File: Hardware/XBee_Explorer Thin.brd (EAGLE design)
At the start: 45.7 x 54.6 mm, 129 parts, among them J4 QWIIC_RIGHT_ANGLE, Q2 3.1A/30V/105mΩ, U1 FSUSB30MUX_MSOP10, U2 AP63203, U3 ESD Diode, U5 ESD Diode, U6 CP210X

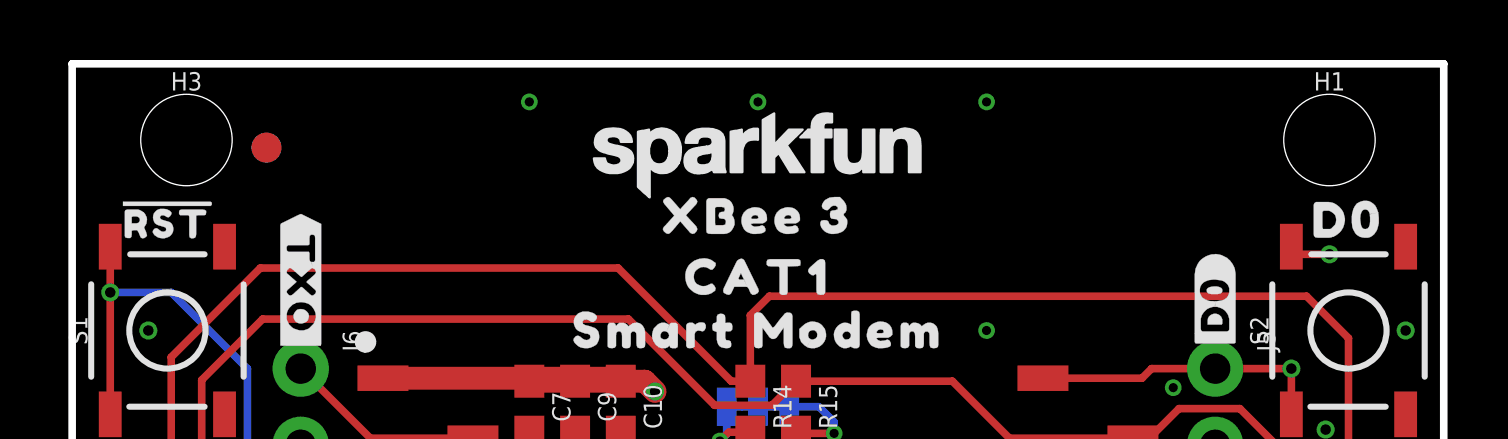
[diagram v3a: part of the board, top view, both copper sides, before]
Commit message: Fixes mounting holes being off grid
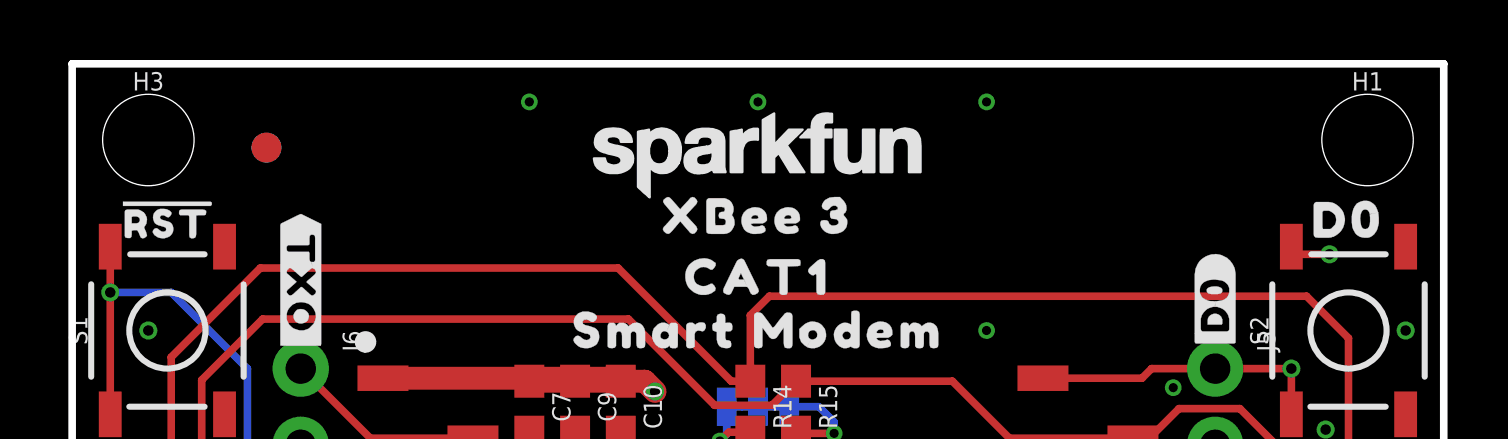
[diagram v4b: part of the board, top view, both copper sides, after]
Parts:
- moved H3 1.27 mm to (1.27, 52.1)
- moved H1 1.27 mm to (41.9, 52.1)
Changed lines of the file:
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@@
 <layer number="37" name="tTest" color="7" fill="1" visible="no" active="yes"/>
 <layer number="38" name="bTest" color="7" fill="1" visible="no" active="yes"/>
-<layer number="39" name="tKeepout" color="4" fill="11" visible="no" active="yes"/>
+<layer number="39" name="tKeepout" color="4" fill="11" visible="yes" active="yes"/>
 <layer number="40" name="bKeepout" color="1" fill="11" visible="no" active="yes"/>
 <layer number="41" name="tRestrict" color="4" fill="10" visible="no" active="yes"/>
@@
 <layer number="45" name="Holes" color="7" fill="1" visible="yes" active="yes"/>
 <layer number="46" name="Milling" color="3" fill="1" visible="no" active="yes"/>
-<layer number="47" name="Measures" color="7" fill="1" visible="no" active="yes"/>
+<layer number="47" name="Measures" color="7" fill="1" visible="yes" active="yes"/>
 <layer number="48" name="Document" color="7" fill="1" visible="no" active="yes"/>
 <layer number="49" name="Reference" color="13" fill="1" visible="yes" active="yes"/>
@@
 </class>
 </classes>
-<designrules name="SparkFun-2-Layer-Minimum-JLCPCB">
-<description language="en">&lt;b&gt;2 Layer Minimum Rules for JLCPCB&lt;/b&gt;
+<designrules name="SparkFun-4-Layer-Minimum-JLCPCB">
+<description language="en">&lt;b&gt;4 Layer Minimum Rules for JLCPCB&lt;/b&gt;
 &lt;p&gt;
-These are the minimums &lt;a href=&quot;https://jlcpcb.com/capabilities/Capabilities&quot;&gt;quoted by JLCPCB&lt;/a&gt; to produce a 2-layer PCB design rules. These rules are &quot;free&quot; and generally low-cost. Going below these settings may cause the board to be not manufacturable or incur a price increase.
+These are the minimums &lt;a href=&quot;https://jlcpcb.com/capabilities/Capabilities&quot;&gt;quoted by JLCPCB&lt;/a&gt; to produce a 4-layer PCB design rules. These rules are &quot;free&quot; and generally low-cost. There is one DRC set that is smaller (see MicroMod rules) but boards designed with these rules should pass review without question.
 &lt;ul&gt;
-&lt;li&gt;2 Layer&lt;/li&gt;
+&lt;li&gt;4 Layer&lt;/li&gt;
 &lt;li&gt;5mil Trace/Space&lt;/li&gt;
 &lt;li&gt;5mil Annular Rings&lt;/li&gt;
-&lt;li&gt;12mil Vias&lt;/li&gt;
+&lt;li&gt;0.2mm/7.9mil Vias&lt;/li&gt;
 &lt;li&gt;2.5mil Stop Mask&lt;/li&gt;
 &lt;/ul&gt;</description>
-<param name="layerSetup" value="(1*16)"/>
-<param name="mtCopper" value="0.035mm 0.035mm 0.035mm 0.035mm 0.035mm 0.035mm 0.035mm 0.035mm 0.035mm 0.035mm 0.035mm 0.035mm 0.035mm 0.035mm 0.035mm 0.035mm"/>
-<param name="mtIsolate" value="1.5mm 0.15mm 0.2mm 0.15mm 0.2mm 0.15mm 0.2mm 0.15mm 0.2mm 0.15mm 0.2mm 0.15mm 0.2mm 0.15mm 0.2mm"/>
+<param name="layerSetup" value="(1*2*15*16)"/>
+<param name="mtCopper" value="0.035559375mm 0.035559375mm 0.035mm 0.035mm 0.035mm 0.035mm 0.035mm 0.035mm 0.035mm 0.035mm 0.035mm 0.035mm 0.035mm 0.035mm 0.035559375mm 0.035559375mm"/>
+<param name="mtIsolate" value="0.47751875mm 0.47751875mm 0.2mm 0.15mm 0.2mm 0.15mm 0.2mm 0.15mm 0.2mm 0.15mm 0.2mm 0.15mm 0.2mm 0.15mm 0.47751875mm"/>
 <param name="mdWireWire" value="5mil"/>
 <param name="mdWirePad" value="5mil"/>
@@
 <param name="mdSmdStop" value="0mil"/>
 <param name="msWidth" value="5mil"/>
-<param name="msDrill" value="0.3mm"/>
+<param name="msDrill" value="0.2mm"/>
 <param name="msMicroVia" value="9.99mm"/>
 <param name="msBlindViaRatio" value="0.5"/>
@@
 <attribute name="VALUE" x="16.256" y="43.18" size="0.6096" layer="27" font="vector" ratio="20" rot="R270" align="top-center"/>
 </element>
-<element name="H1" library="SparkFun-Hardware" package="STAND-OFF-TIGHT" value="STAND-OFFTIGHT" x="40.64" y="52.07" smashed="yes">
-<attribute name="NAME" x="40.64" y="53.721" size="0.6096" layer="25" font="vector" ratio="20" align="bottom-center"/>
-<attribute name="VALUE" x="40.64" y="50.419" size="0.6096" layer="27" font="vector" ratio="20" align="top-center"/>
+<element name="H1" library="SparkFun-Hardware" package="STAND-OFF-TIGHT" value="STAND-OFFTIGHT" x="41.91" y="52.07" smashed="yes">
+<attribute name="NAME" x="41.91" y="53.721" size="0.6096" layer="25" font="vector" ratio="20" align="bottom-center"/>
+<attribute name="VALUE" x="41.91" y="50.419" size="0.6096" layer="27" font="vector" ratio="20" align="top-center"/>
 </element>
 <element name="H2" library="SparkFun-Hardware" package="STAND-OFF-TIGHT" value="STAND-OFFTIGHT" x="41.91" y="2.54" smashed="yes">
@@
 <attribute name="VALUE" x="41.91" y="0.889" size="0.6096" layer="27" font="vector" ratio="20" align="top-center"/>
 </element>
-<element name="H3" library="SparkFun-Hardware" package="STAND-OFF-TIGHT" value="STAND-OFFTIGHT" x="2.54" y="52.07" smashed="yes">
-<attribute name="NAME" x="2.54" y="53.721" size="0.6096" layer="25" font="vector" ratio="20" align="bottom-center"/>
-<attribute name="VALUE" x="2.54" y="50.419" size="0.6096" layer="27" font="vector" ratio="20" align="top-center"/>
+<element name="H3" library="SparkFun-Hardware" package="STAND-OFF-TIGHT" value="STAND-OFFTIGHT" x="1.27" y="52.07" smashed="yes">
+<attribute name="NAME" x="1.27" y="53.721" size="0.6096" layer="25" font="vector" ratio="20" align="bottom-center"/>
+<attribute name="VALUE" x="1.27" y="50.419" size="0.6096" layer="27" font="vector" ratio="20" align="top-center"/>
 </element>
 <element name="H4" library="SparkFun-Hardware" package="STAND-OFF-TIGHT" value="STAND-OFFTIGHT" x="1.27" y="2.54" smashed="yes">

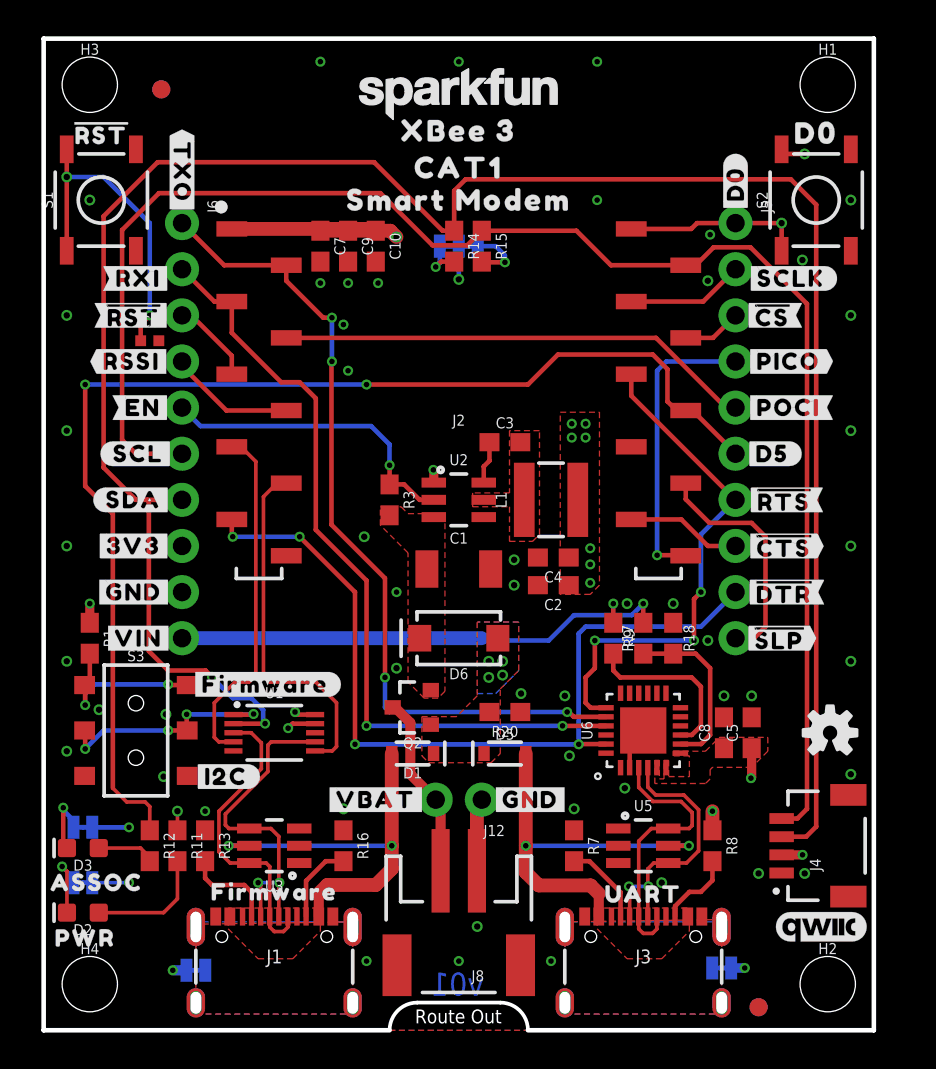
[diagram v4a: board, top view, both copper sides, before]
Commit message: Replaces the only 0402 on the board with an 0603, replaces only 100k resistor with a 10k, fixes input/ouput labeling
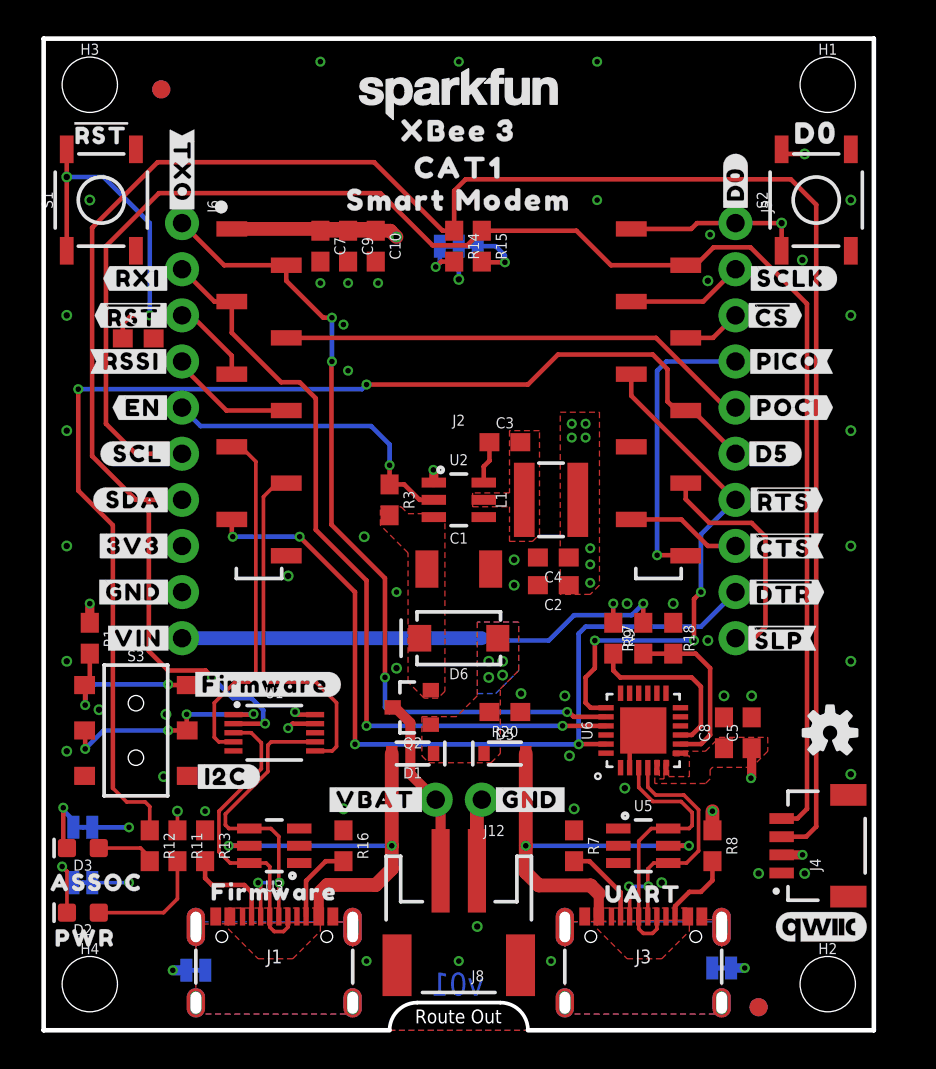
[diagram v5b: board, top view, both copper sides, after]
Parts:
- C6: device SparkFun-Capacitors:0402-TIGHT -> SparkFun-Capacitors:0603
- R3: value 100k -> 10k
- U$28: device top:#PICO#21 -> top:#PICO#23
- U$29: device top:#POCI#20 -> top:#POCI#22
- U$4: device top:##CTS##23 -> top:##CTS##25
- U$47: device top:##SLP##25 -> top:##SLP##27
- U$5: device top:##DTR##24 -> top:##DTR##26
- U$7: device top:##RTS##22 -> top:##RTS##24
- moved C6 0.65 mm to (3.94, 38.1)
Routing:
- net !RESET!: track 24.4 -> 25.2 mm
- net D1/SCL: track 87.2 -> 87.9 mm
- net D11/SDA: track 118.9 -> 119.4 mm
- net GND: vias 57 -> 58

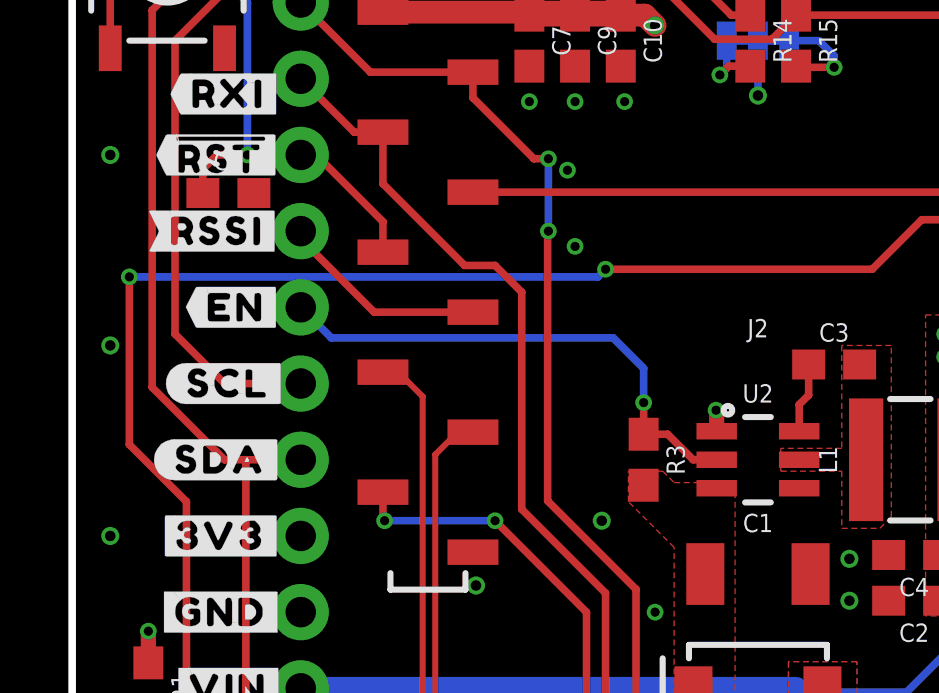
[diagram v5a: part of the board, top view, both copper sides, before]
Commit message: Fixes DRC issue
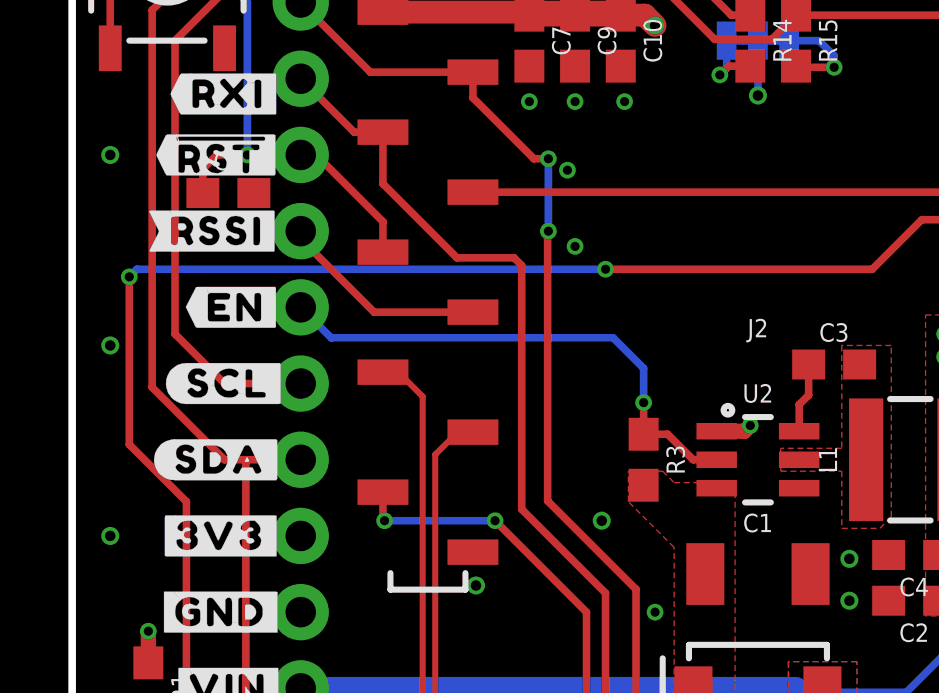
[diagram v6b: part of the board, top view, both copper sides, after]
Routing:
- net D14/RXI: track 43.7 -> 44.2 mm
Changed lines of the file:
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@@
 <via x="1.27" y="23.495" extent="1-16" drill="0.3048"/>
 <wire x1="1.27" y1="22.44" x2="1.27" y2="23.495" width="0.508" layer="1"/>
-<wire x1="20.2149" y1="30.16" x2="20.2149" y2="30.8391" width="0.508" layer="1"/>
-<wire x1="20.2149" y1="30.8391" x2="20.193" y2="30.861" width="0.508" layer="1"/>
-<via x="20.193" y="30.861" extent="1-16" drill="0.3048"/>
+<wire x1="20.2149" y1="30.16" x2="21.143" y2="30.16" width="0.508" layer="1"/>
+<wire x1="21.336" y1="30.353" x2="21.143" y2="30.16" width="0.508" layer="1"/>
+<via x="21.336" y="30.353" extent="1-16" drill="0.3048"/>
 <via x="28.829" y="25.654" extent="1-16" drill="0.3048"/>
 <via x="28.829" y="26.543" extent="1-16" drill="0.3048"/>
@@
 <via x="18.161" y="43.688" extent="1-16" drill="0.35"/>
 <wire x1="17.819" y1="44.03" x2="17.018" y2="44.03" width="0.762" layer="1"/>
-<wire x1="20.193" y1="30.861" x2="20.193" y2="31.75" width="0.762" layer="2"/>
-<wire x1="21.844" y1="33.401" x2="27.813" y2="33.401" width="0.762" layer="2"/>
-<wire x1="20.193" y1="31.75" x2="21.844" y2="33.401" width="0.762" layer="2"/>
+<wire x1="21.336" y1="30.353" x2="21.336" y2="31.75" width="0.762" layer="2"/>
+<wire x1="22.987" y1="33.401" x2="27.813" y2="33.401" width="0.762" layer="2"/>
+<wire x1="21.336" y1="31.75" x2="22.987" y2="33.401" width="0.762" layer="2"/>
 </signal>
 <signal name="V_USB">
@@
 <via x="16.51" y="16.764" extent="1-16" drill="0.3048"/>
 <wire x1="16.51" y1="16.764" x2="16.51" y2="24.765" width="0.254" layer="1"/>
-<wire x1="13.716" y1="27.559" x2="13.716" y2="34.798" width="0.254" layer="1"/>
+<wire x1="13.716" y1="27.559" x2="13.716" y2="35.687" width="0.254" layer="1"/>
 <wire x1="16.51" y1="24.765" x2="13.716" y2="27.559" width="0.254" layer="1"/>
-<wire x1="13.716" y1="34.798" x2="12.827" y2="35.687" width="0.254" layer="1"/>
-<wire x1="12.827" y1="35.687" x2="11.811" y2="35.687" width="0.254" layer="1"/>
+<wire x1="13.716" y1="35.687" x2="13.462" y2="35.941" width="0.254" layer="1"/>
+<wire x1="13.462" y1="35.941" x2="11.557" y2="35.941" width="0.254" layer="1"/>
 <contactref element="J6" pad="2"/>
-<wire x1="11.811" y1="35.687" x2="9.09" y2="38.408" width="0.254" layer="1"/>
+<wire x1="11.557" y1="35.941" x2="9.09" y2="38.408" width="0.254" layer="1"/>
 <wire x1="9.09" y1="38.408" x2="9.09" y2="40.13" width="0.254" layer="1"/>
 <wire x1="9.09" y1="40.13" x2="8.13" y2="40.13" width="0.254" layer="1"/>
@@
 <wire x1="32.2782125" y1="37.211" x2="33.083" y2="36.4062125" width="0.254" layer="1"/>
 <via x="16.51" y="35.56" extent="1-16" drill="0.3048"/>
-<wire x1="16.51" y1="35.56" x2="16.256" y2="35.306" width="0.254" layer="16"/>
-<wire x1="16.256" y1="35.306" x2="0.635" y2="35.306" width="0.254" layer="16"/>
+<wire x1="16.51" y1="35.56" x2="0.889" y2="35.56" width="0.254" layer="16"/>
+<wire x1="0.889" y1="35.56" x2="0.635" y2="35.306" width="0.254" layer="16"/>
 <via x="0.635" y="35.306" extent="1-16" drill="0.3048"/>
 <wire x1="0.635" y1="35.306" x2="0.635" y2="29.718" width="0.254" layer="1"/>
